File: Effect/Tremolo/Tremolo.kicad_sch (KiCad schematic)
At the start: 28 parts, among them J1 Conn_01x04_Pin, J2 Conn_01x03_Pin, Q1 MBT2222ADW1T1, Q2 MBT2222ADW1T1

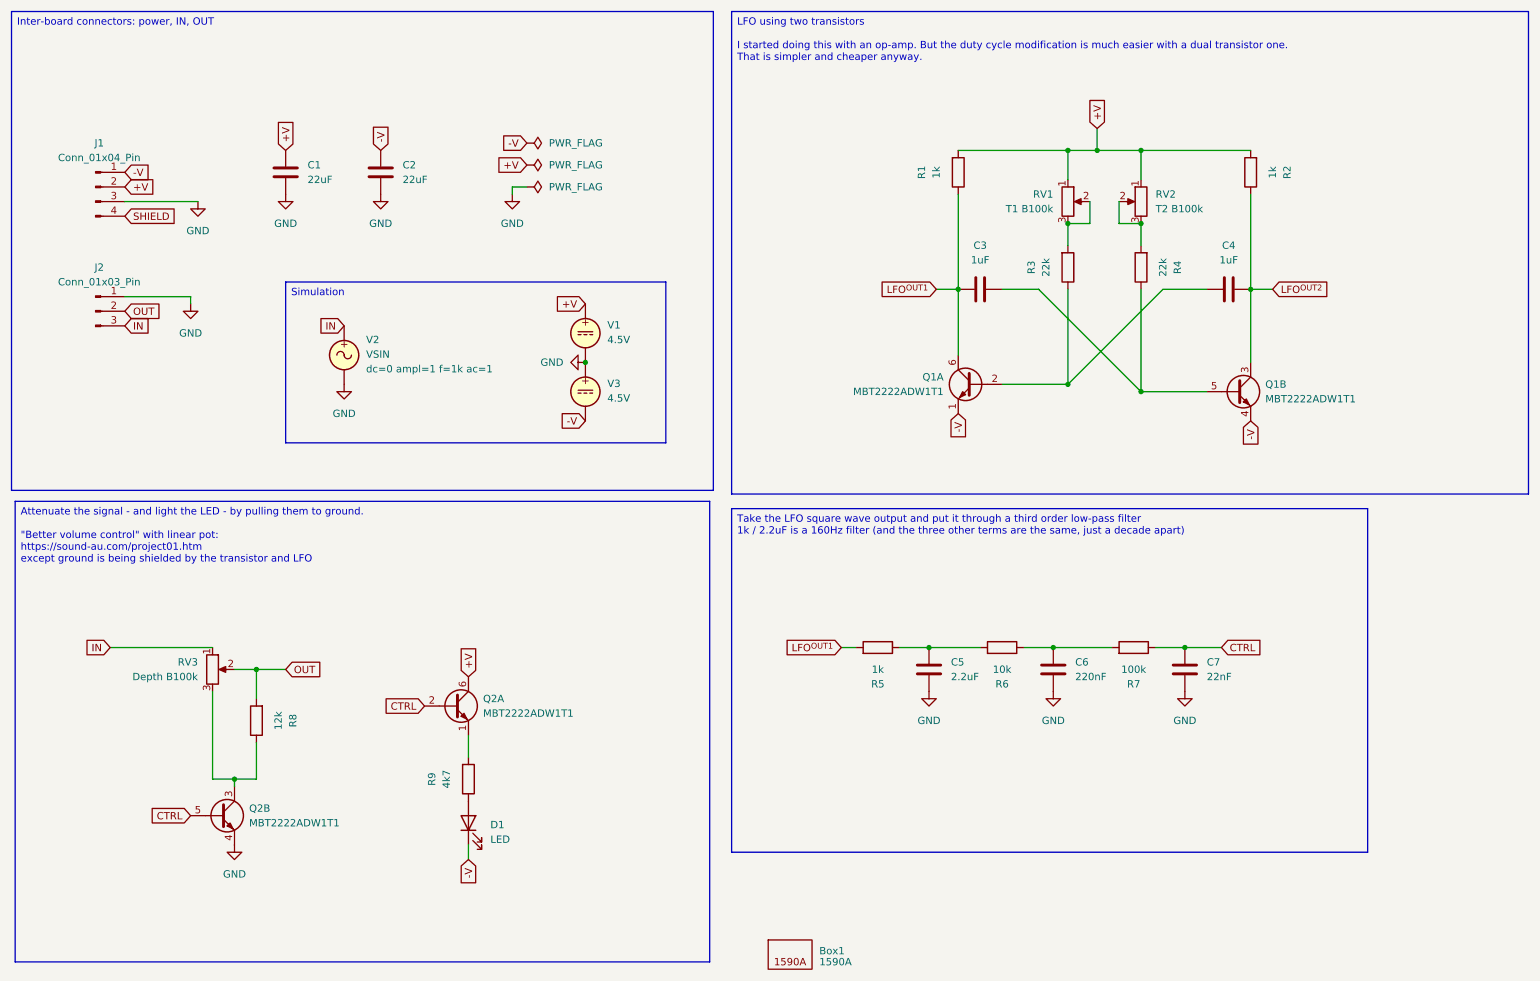
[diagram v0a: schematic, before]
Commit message: Updated Tremolo board, version N+1
I'm not sure this is a particularly good tremolo, but it's been an
absolutely stellar board for learning about transistors.

It started out using an op-amp for the oscillator, and the P-MOSFET that
I used for reverse voltage protection as the attenuator.  And that
worked, with some popping noise ("Tremolo doubling as a metronome" #4).

Which was fixed with a nicer driving curve, and the popping went from
"metronome" to "there's still some 'fizz' sound modulated by the
oscillator frequency.  But I also wanted to make sure I could change the
timing more conveniently and have different duty cycles, so I ignored
that and went back to the drawing board.

Then the op-amp circuit was replaced with just a dual transistor
bistable oscillator instead using dual BJT transistors, because that
made the timing much simpler and more flexible.  And in the process, I
did the signal attenuation and the LED driving with another dual BJT,
because why not?

And then the third stage answers the "Why not?" question.  Because it
turns out the BJT as the transistor pulling down to ground didn't work
so well and that was likely also the cause of the 'fizz' with the MOSFET version.

So now I'm using a JFET for that, a separate BJT for the LED, and the
dual BJT still does the oscillator part.

I've got a couple of different JFET's on order: the MMBF4393LT1G was
suggested by Eric Kuzmenko (@gralco), and looks good.  And after looking
at way too many other ones tryin gto figure out the differences, I'm
also going to try the MMBF5103.  Same D/S/G ordering in a SOT-23, so
they are interchangeable.

The MMBF5103 simulates slightly better and hopefully this also fixes the
fizz issue for good.  But let's see if that actually shows up in
reality.

Signed-off-by: Linus Torvalds <torvalds@linux-foundation.org>
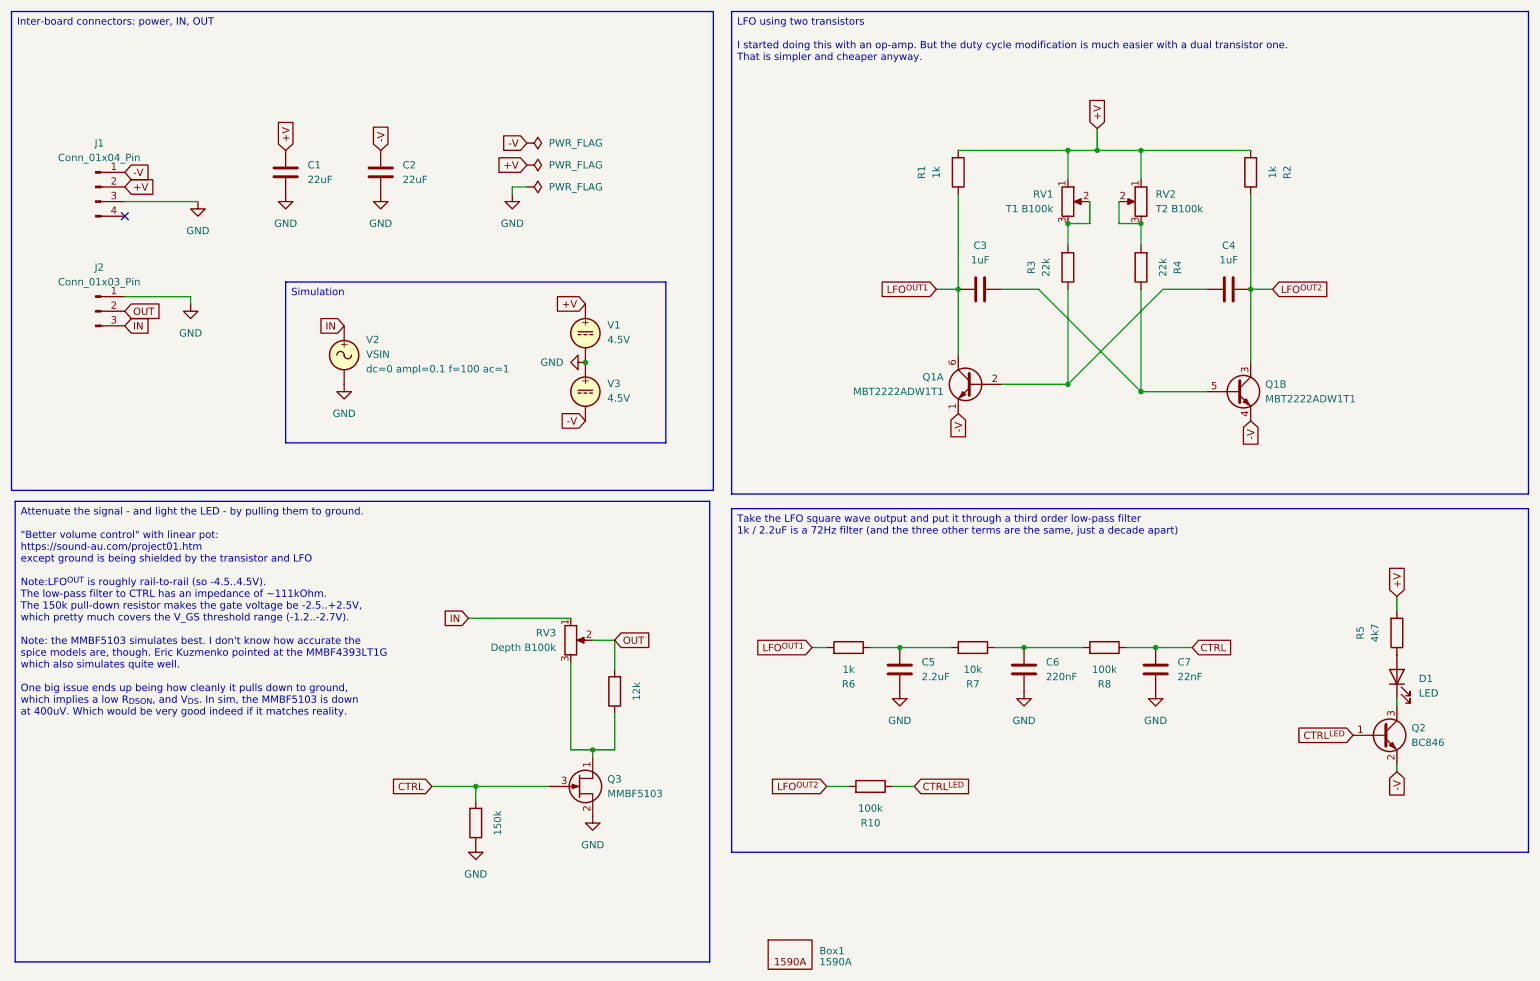
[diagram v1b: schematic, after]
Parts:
- removed Q2: MBT2222ADW1T1, Package_TO_SOT_SMD:SOT-363_SC-70-6, symbol Transistor_BJT:MBT2222ADW1T1
- added Q2: BC846, Package_TO_SOT_SMD:SOT-23, symbol Transistor_BJT:BC846
- added Q3: MMBF5103, Package_TO_SOT_SMD:SOT-23, symbol Device:Q_NJFET_DSG
- added R10: 100k, Resistor_SMD:R_0805_2012Metric_Pad1.20x1.40mm_HandSolder, symbol Device:R
- added R11: 150k, Resistor_SMD:R_0805_2012Metric_Pad1.20x1.40mm_HandSolder, symbol Device:R
- renumbered R9 to R5, R5 to R6, R6 to R7, R7 to R8, R8 to R9
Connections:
- net +V: now also R5.2
- net -V: now also Q2.2 (E); no longer D1.1 (K)
- net CTRL: now also Q3.3 (G), R11.2
- net GND: now also Q3.2 (S), R11.1
- net LFO^{OUT2}: now also R10.2
- net at R9.1, RV3.3: now also Q3.1 (D)
- net SHIELD: no longer names the net of J1.4 (Pin_4)
- new net: D1.1 (K), Q2.3 (C)
- new net CTRL^{LED}: Q2.1 (B), R10.1
- no-connect marks 0 -> 1
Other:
- moved on the sheet: C5, C6, C7, D1, R5, R6, R7, R8, RV3

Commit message: Use the new 9mm pot footprint in the tremolo board
Mainly just checking that it works at all. Seems fine.

Signed-off-by: Linus Torvalds <torvalds@linux-foundation.org>
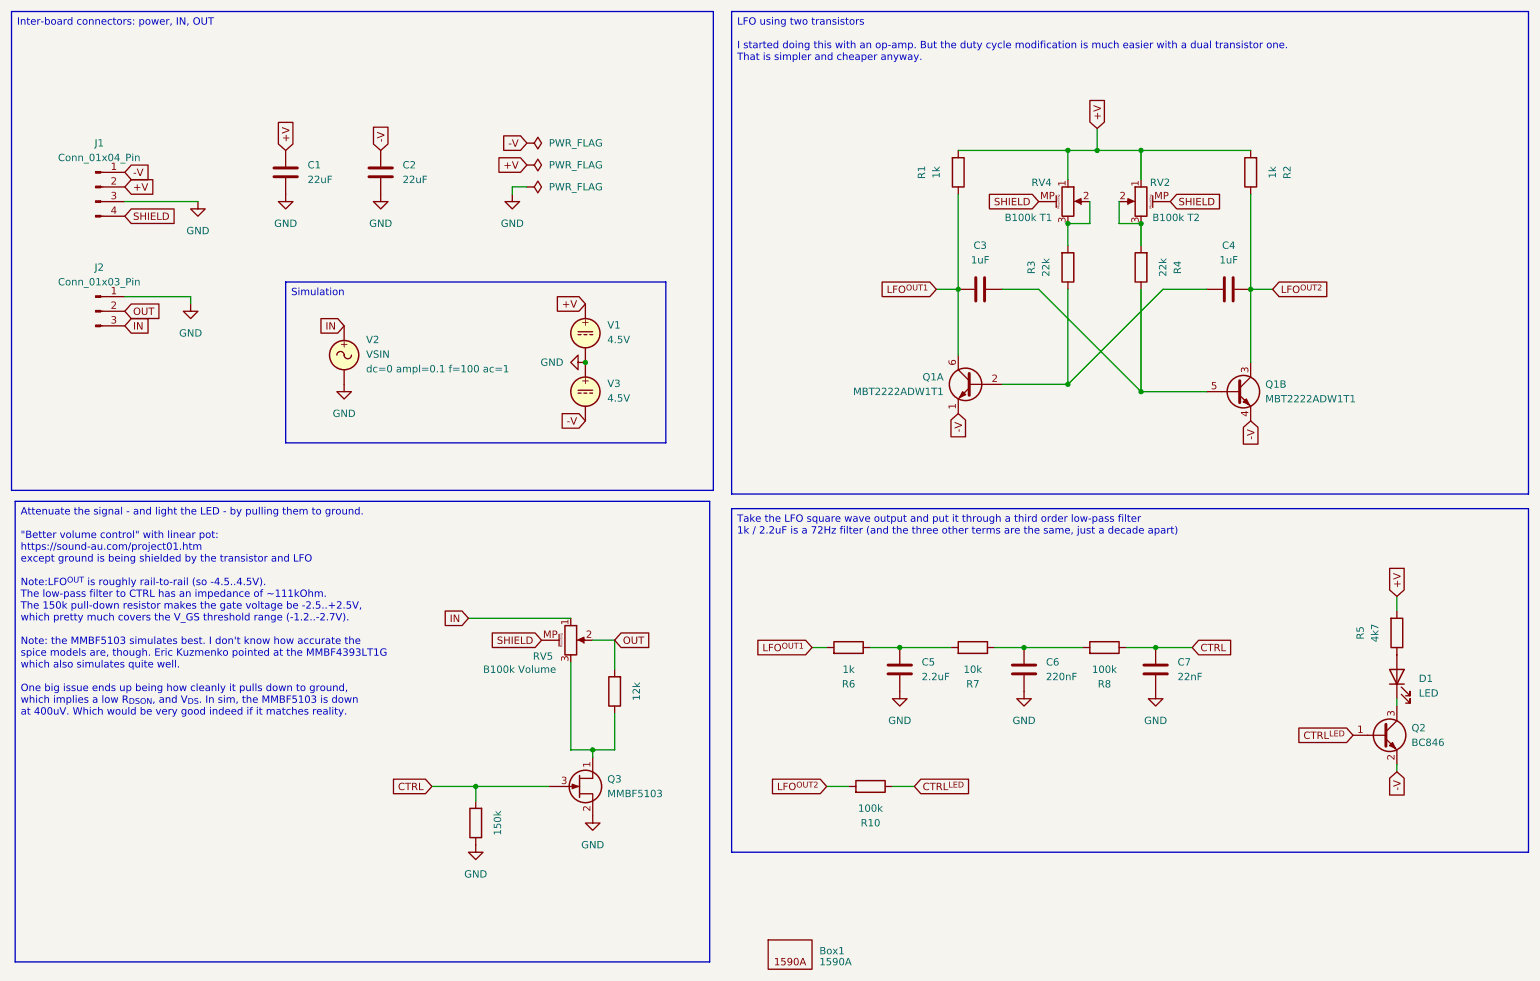
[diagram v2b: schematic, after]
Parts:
- removed RV1: T1 B100k, Potentiometer_THT:Potentiometer_Alpha_RD901F-40-00D_Single_Vertical, symbol Device:R_Potentiometer
- removed RV2: T2 B100k, Potentiometer_THT:Potentiometer_Alpha_RD901F-40-00D_Single_Vertical, symbol Device:R_Potentiometer
- removed RV3: Depth B100k, Potentiometer_THT:Potentiometer_Alpha_RD901F-40-00D_Single_Vertical, symbol Device:R_Potentiometer
- added RV2: B100k T2, Mylib:Potentiometer_9mm_MP, symbol Device:R_Potentiometer_MountingPin
- added RV4: B100k T1, Mylib:Potentiometer_9mm_MP, symbol Device:R_Potentiometer_MountingPin
- added RV5: B100k Volume, Mylib:Potentiometer_9mm_MP, symbol Device:R_Potentiometer_MountingPin
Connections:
- net +V: now also RV2.1, RV4.1
- net IN: now also RV5.1
- net OUT: now also RV5.2
- net at Q3.1 (D), R9.1: now also RV5.3
- net at R3.2: now also RV4.2, RV4.3
- net at R4.2: now also RV2.2, RV2.3
- net SHIELD: now reaches J1.4 (Pin_4)
- net SHIELD: now also RV2.MP (MountPin), RV4.MP (MountPin), RV5.MP (MountPin)
- no-connect marks 1 -> 0

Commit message: Use the JFET to switch the signal, not pull it to ground
I really thought I was being clever by combining the voluem control with
pulling the signal to the ground through the transistor.  But it turns
out I just can't fix the noise that this introduces by basically making
the transistor voltage be part of the path to ground.

Maybe it's fixable some other way, but I have seen the error of my "try
to be clever" ways, and am instead just using the JFET in a much simpler
capacity as just a direct analog switch.  That seems to work much
better.

That does mean that now the "depth" knob that used to control the signal
modulation strength is just a passive volume knob, and is as such
entirely useless.

The "clever" part of the pull-down-to-ground thing was how I avoided any
signal blending circuitry, because it was a "sometimes we pull down to
ground, sometimes we don't" and the blend pot just changed how _hard_ it
was pulled down to ground.

Now I'll have to replace that with a "how much to blend in the original
signal" instead, but at least I know how to do that, even if this commit
doesn't do it yet.

Signed-off-by: Linus Torvalds <torvalds@linux-foundation.org>
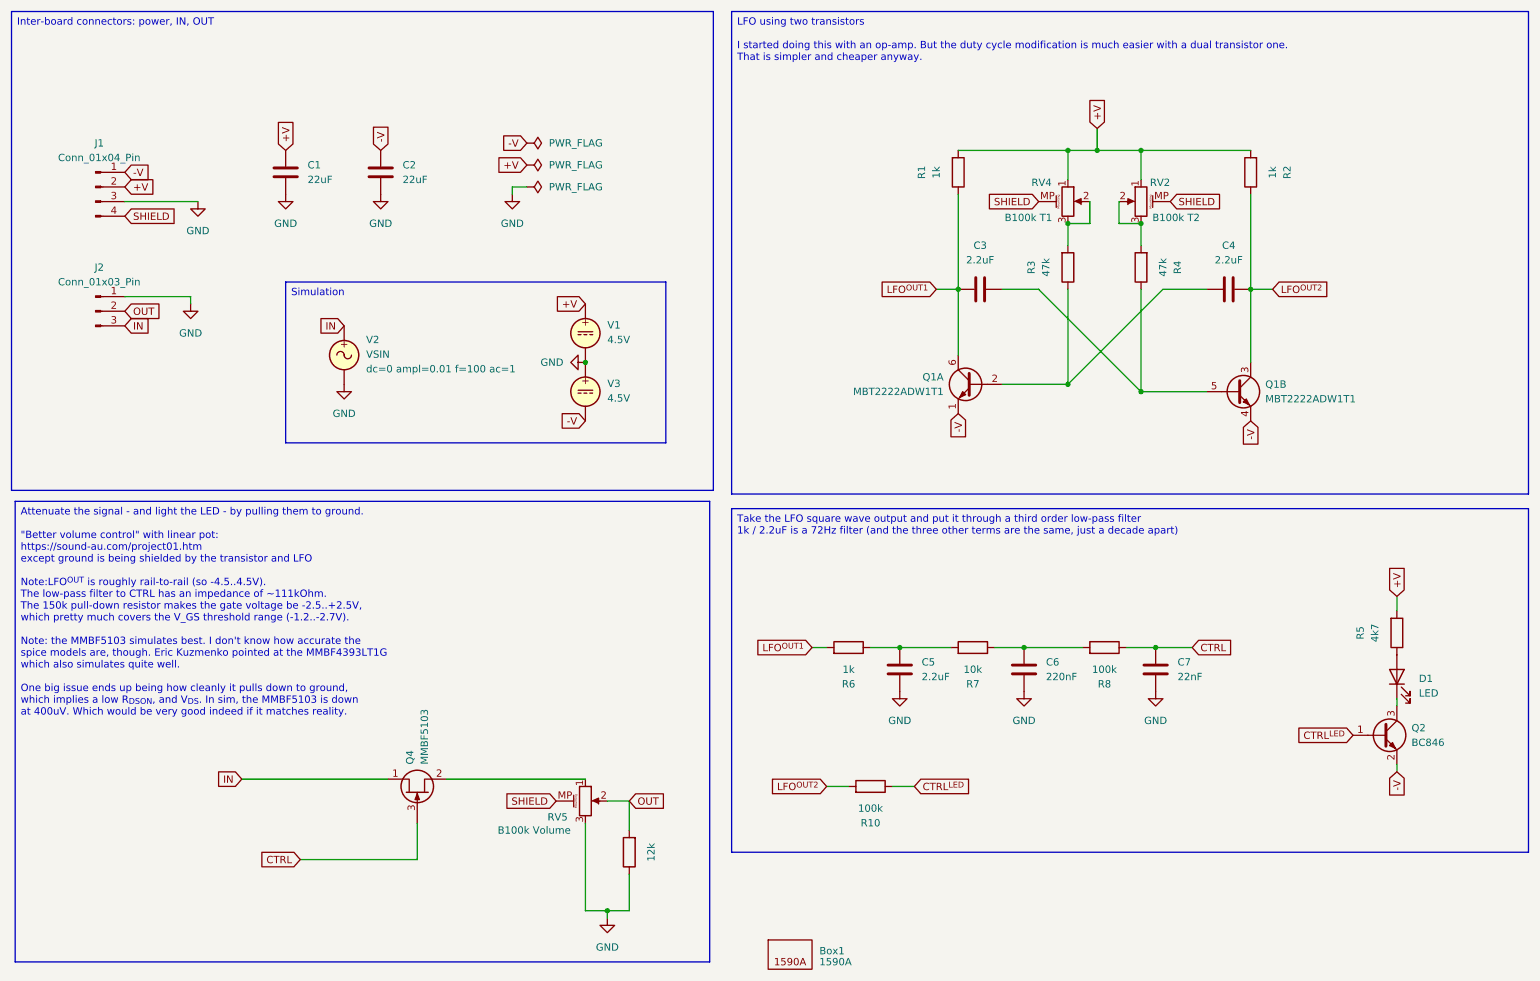
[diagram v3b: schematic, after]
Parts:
- removed Q3: MMBF5103, Package_TO_SOT_SMD:SOT-23, symbol Device:Q_NJFET_DSG
- removed R11: 150k, Resistor_SMD:R_0805_2012Metric_Pad1.20x1.40mm_HandSolder, symbol Device:R
- added Q4: MMBF5103, Package_TO_SOT_SMD:SOT-23, symbol Device:Q_NJFET_DSG
- C3, C4: value 1uF -> 2.2uF
- R3, R4: value 22k -> 47k
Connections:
- net CTRL: now also Q4.3 (G)
- net GND: now also R9.1, RV5.3
- net IN: now also Q4.1 (D); no longer RV5.1
- new net: Q4.2 (S), RV5.1
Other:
- moved on the sheet: RV5
